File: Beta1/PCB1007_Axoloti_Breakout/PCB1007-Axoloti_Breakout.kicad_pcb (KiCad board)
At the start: 2 copper layers, 160 x 48 mm, 43 parts, among them J1 Axoloti_40Pin, U10 OLED_128x32_I2C, U1000 MCP3008T-I/SL, U2 MCP3008T-I/SL, U20 OLED_128x32_I2C, U30 OLED_128x32_I2C, U40 OLED_128x32_I2C, U5 I2C_1x4MUX_TCA9546A

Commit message: SCH+Route complete
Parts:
- removed C1, C1000, C2: 0.1u, Capacitors_SMD:C_0603
- removed JOY0, JOY1, JOY2, JOY3: XYJOY, Liberry:XY_JOY_254TA103B50B
- removed RC0, RC10, RC20, RC30, RC40, RD0, RD10, RD20, RD30, RD40, RR0: 10K, Resistors_SMD:R_0603
- removed the REF** at (44.0, -10.0)
- removed RV0, RV1, RV2, RV3, RV4, RV5, RV6, RV7, RV_VOL1: POT, Liberry:RV09AF-40-20K-B10K
- removed U10, U20, U30, U40: OLED_128x32_I2C, Liberry:OLED_128x32
- removed U1000, U2: MCP3008T-I/SL, Liberry:SOIC-16
- removed U5: I2C_1x4MUX_TCA9546A, Liberry:SOIC-16_1.27x5.4
- added JK0: USB-K, Liberry:USB-K_12401610E4_2A, F.Cu at (8.60, -25.4)
- added REF**: Fiducial_1mm_Dia_2.54mm_Outer_CopperTop, Fiducials:Fiducial_1mm_Dia_2.54mm_Outer_CopperTop, F.Cu at (12.7, -7.62)
- added REF**: Fiducial_1mm_Dia_2.54mm_Outer_CopperTop, Fiducials:Fiducial_1mm_Dia_2.54mm_Outer_CopperTop, F.Cu at (12.7, -35.6)
- added REF**: 1pin, Connect:1pin, F.Cu at (44.0, -10.0)
- added REF**: 1pin, Connect:1pin, F.Cu at (3.50, -10.0)
- added TEST0: CONN_01X01, Liberry:TH_0.1_1x2_Jumper, F.Cu at (22.9, -43.2)
- added TEST1: CONN_01X01, Liberry:TH_0.1_1x2_Jumper, F.Cu at (22.9, -45.7)
- added TEST2: CONN_01X01, Liberry:TH_0.1_1x2_Jumper, F.Cu at (22.9, -40.6)
- moved REF** 38.2 mm to (2.54, -35.6)
- moved REF** 30.0 mm to (3.50, -40.0)
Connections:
- J1 pad 11: /JOY_K0 -> /JOY0
- J1 pad 12: /JOY_K1 -> /JOY1
- J1 pad 18: Net-(J1-Pad18) -> /TX
- J1 pad 19: Net-(J1-Pad19) -> /RX
- J1 pad 8: /JOY_0_SW -> /JOY_SW
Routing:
- net +3V3: track 618.9 -> 275.5 mm
- net /P0: track 132.1 -> 0.00 mm, vias 1 -> 0
- net /JOY_0_1: track 125.4 -> 0.00 mm, vias 1 -> 0
- net /RX: track 0.00 -> 113.3 mm, vias 0 -> 1
- net /TX: track 0.00 -> 111.9 mm, vias 0 -> 1
- net /P1: track 108.5 -> 0.00 mm, vias 1 -> 0
- net GND: track 166.7 -> 59.3 mm, vias 3 -> 1
- net /JOY0: track 0.00 -> 106.4 mm, vias 0 -> 1
- net /JOY_0_0: track 101.9 -> 0.00 mm, vias 1 -> 0
- net /I2C_SDA3: track 99.3 -> 0.00 mm
- net /JOY1: track 0.00 -> 97.6 mm
- net /I2C_SCL3: track 95.8 -> 0.00 mm
- net /JOY_SW: track 0.00 -> 87.7 mm, vias 0 -> 1
- net /JOY_1_1: track 75.3 -> 0.00 mm, vias 1 -> 0
- net /P2: track 70.2 -> 0.00 mm, vias 3 -> 0
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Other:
- board text added: "PCB1007_USB-K Breakout 2017-07-08 https://github.com/Believotron/BelievotronWanderlustHardware"
- board text removed: "254TA103B50B"
- board text removed: "All R=10KΩ All C=0.1uF"
- board text removed: "MCP3008T-I/SL"
- board text removed: "PCB1005_KnobCore_2017-07-06 8CH Knobs + Vol + 4CH JoyXY + 4CH OLED https://github.com/Believotron/BelievotronWanderlustHardware"
- board text removed: "RV09AF-40-20K-B10K"
- board text removed: "TCA9546ADR"

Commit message: PCB1006 Ready for fab
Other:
- board text added: "PCB1007_USB-K Breakout 2017-07-11 https://github.com/Believotron/BelievotronWanderlustHardware"
- board text removed: "PCB1007_USB-K Breakout 2017-07-08 https://github.com/Believotron/BelievotronWanderlustHardware"
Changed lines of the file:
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@@
     (links 118)
     (no_connects 1)
-    (area -0.050001 -48.050001 160.050001 0.050001)
+    (area -14.398096 -50.8 185.860001 0.100001)
     (thickness 1.6)
     (drawings 17)
@@
       (drillshape 0)
       (scaleselection 1)
-      (outputdirectory PCB1005-KnobCore_Gerbers_2017-06-07/))
+      (outputdirectory PCB1007-Axoloti_USB-K_2017-07-11_Gerbers/))
   )
   (net 0 "")
@@
     (effects (font (size 1.15 1.15) (thickness 0.15)))
   )
-  (gr_text "PCB1007_USB-K Breakout 2017-07-08\nhttps://github.com/Believotron/BelievotronWanderlustHardware\n" (at 0.635 -2.54) (layer F.SilkS)
+  (gr_text "PCB1007_USB-K Breakout 2017-07-11\nhttps://github.com/Believotron/BelievotronWanderlustHardware\n" (at 0.635 -2.54) (layer F.SilkS)
     (effects (font (size 1 1) (thickness 0.15)) (justify left))
   )

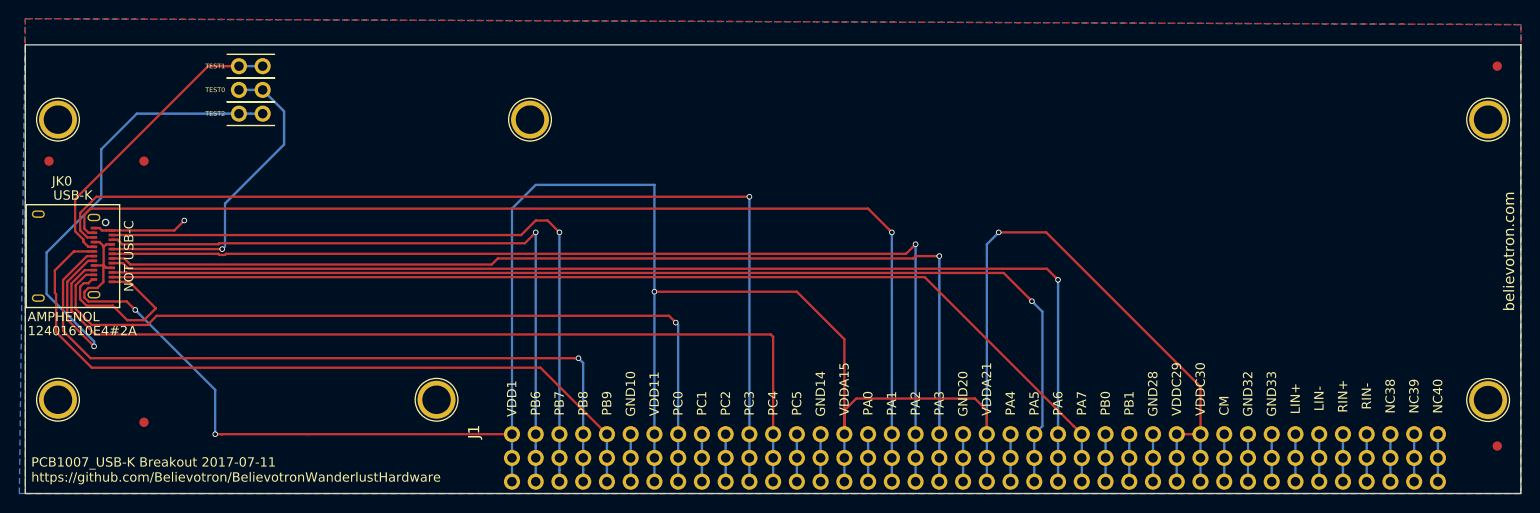
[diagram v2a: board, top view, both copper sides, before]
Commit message: Conversion to FFC WIP
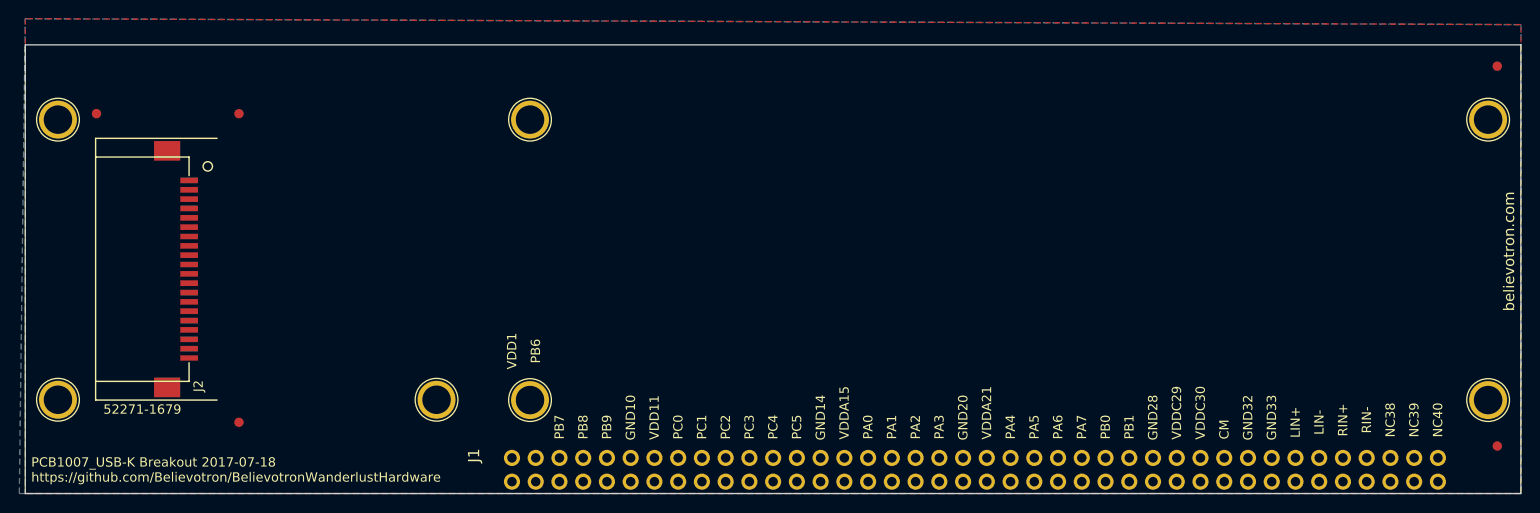
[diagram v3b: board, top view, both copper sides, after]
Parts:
- removed JK0: USB-K, Liberry:USB-K_12401610E4_2A
- removed TEST0, TEST1, TEST2: CONN_01X01, Liberry:TH_0.1_1x2_Jumper
- added J2: FPC_20POS, Liberry:FFC_1MM_20POS_MOLEX_52271-2079, F.Cu at (17.5, -24.0)
- added REF**: 1pin, Connect:1pin, F.Cu at (54.0, -10.0)
- J1: footprint Liberry:Axoloti-40x3_slim -> Liberry:Axoloti-40x2_slim
- moved REF** 11.4 mm to (22.9, -40.6)
- moved REF** 10.2 mm to (22.9, -7.62)
- moved REF** 7.18 mm to (7.62, -40.6)
- moved J1 2.54 mm to (52.1, -1.27)
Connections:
- net /JOY_2_SW renamed Net-(J1-Pad26)
- net /JOY_3_SW renamed Net-(J1-Pad27)
- net /JOY_K_SW renamed Net-(J1-Pad16)
- J1 pad 11: /JOY0 -> /JOY0_X
- J1 pad 12: /JOY1 -> /JOY0_Y
- J1 pad 13: Net-(J1-Pad13) -> /JOY0_SW
- J1 pad 22: Net-(J1-Pad22) -> /ANALOG_OUT
- J1 pad 8: /JOY_SW -> /PC0
- J1 pad 9: /JOY_1_SW -> /PC1
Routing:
- net +3V3: track 275.5 -> 0.00 mm, vias 4 -> 0
- net /SPI_MISO: track 123.6 -> 0.00 mm, vias 1 -> 0
- net /SPI_CLK: track 119.8 -> 0.00 mm, vias 1 -> 0
- net /VOLUME: track 117.1 -> 0.00 mm, vias 1 -> 0
- net /SPI_MOSI: track 115.8 -> 0.00 mm
- net /RX: track 113.3 -> 0.00 mm, vias 1 -> 0
- net /TX: track 111.9 -> 0.00 mm, vias 1 -> 0
- net /JOY0: track 106.4 -> 0.00 mm, vias 1 -> 0
- net /JOY1: track 97.6 -> 0.00 mm
- net /JOY_SW: track 87.7 -> 0.00 mm, vias 1 -> 0
- net /I2C_SDA: track 80.2 -> 0.00 mm
- net /I2C_SCL: track 79.6 -> 0.00 mm, vias 1 -> 0
- net /CS_0_7: track 75.7 -> 0.00 mm, vias 1 -> 0
- net /CS_8_15: track 72.7 -> 0.00 mm, vias 1 -> 0
- net GND: track 59.3 -> 0.00 mm, vias 1 -> 0
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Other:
- board text added: "PCB1007_USB-K Breakout 2017-07-18 https://github.com/Believotron/BelievotronWanderlustHardware"
- board text removed: "PCB1007_USB-K Breakout 2017-07-11 https://github.com/Believotron/BelievotronWanderlustHardware"

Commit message: Added 20 pos FFC
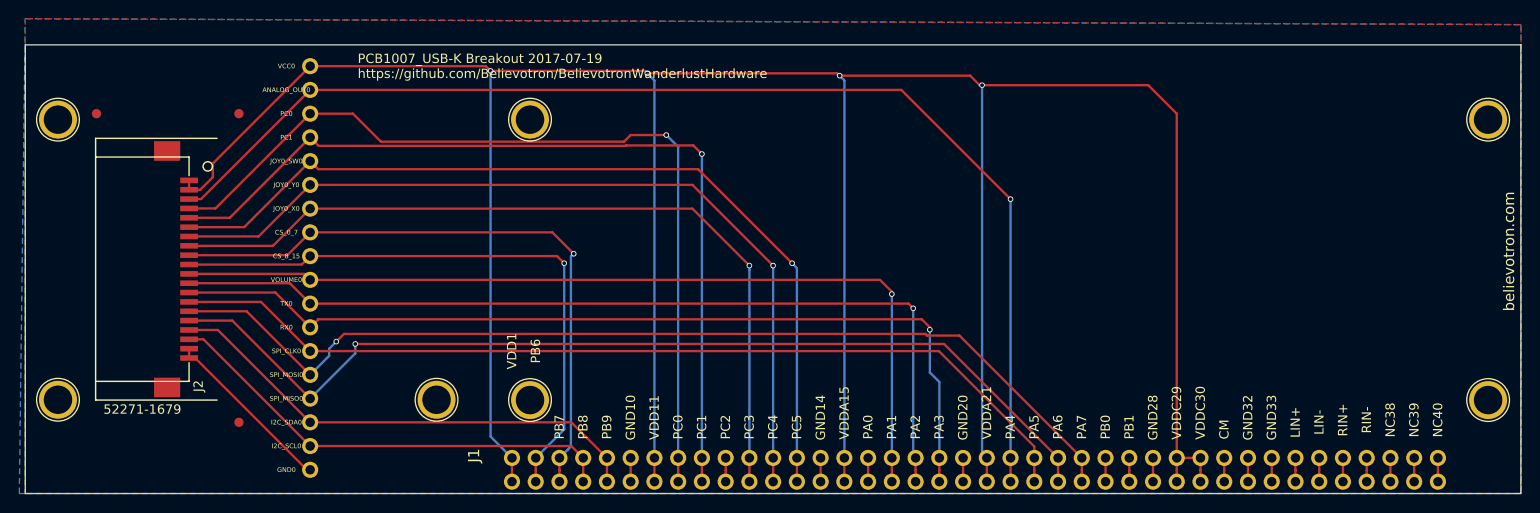
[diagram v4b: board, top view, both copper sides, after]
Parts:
- removed the REF** at (157.5, -5.08)
- removed the REF** at (157.5, -45.7)
- added ANALOG_OUT0: CONN_01X01, Liberry:single_0.1, F.Cu at (30.5, -43.2)
- added CS_0_7: CONN_01X01, Liberry:single_0.1, F.Cu at (30.5, -27.9)
- added CS_8_15: CONN_01X01, Liberry:single_0.1, F.Cu at (30.5, -25.4)
- added GND0: CONN_01X01, Liberry:single_0.1, F.Cu at (30.5, -2.54)
- added I2C_SCL0: CONN_01X01, Liberry:single_0.1, F.Cu at (30.5, -5.08)
- added I2C_SDA0: CONN_01X01, Liberry:single_0.1, F.Cu at (30.5, -7.62)
- added JOY0_SW0: CONN_01X01, Liberry:single_0.1, F.Cu at (30.5, -35.6)
- added JOY0_X0: CONN_01X01, Liberry:single_0.1, F.Cu at (30.5, -30.5)
- added JOY0_Y0: CONN_01X01, Liberry:single_0.1, F.Cu at (30.5, -33.0)
- added PC0: CONN_01X01, Liberry:single_0.1, F.Cu at (30.5, -40.6)
- added PC1: CONN_01X01, Liberry:single_0.1, F.Cu at (30.5, -38.1)
- added RX0: CONN_01X01, Liberry:single_0.1, F.Cu at (30.5, -17.8)
- added SPI_CLK0: CONN_01X01, Liberry:single_0.1, F.Cu at (30.5, -15.2)
- added SPI_MISO0: CONN_01X01, Liberry:single_0.1, F.Cu at (30.5, -10.2)
- added SPI_MOSI0: CONN_01X01, Liberry:single_0.1, F.Cu at (30.5, -12.7)
- added TX0: CONN_01X01, Liberry:single_0.1, F.Cu at (30.5, -20.3)
- added VCC0: CONN_01X01, Liberry:single_0.1, F.Cu at (30.5, -45.7)
- added VOLUME0: CONN_01X01, Liberry:single_0.1, F.Cu at (30.5, -22.9)
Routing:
- net +3V3: track 0.00 -> 334.7 mm, vias 0 -> 4
- net /ANALOG_OUT: track 0.00 -> 127.8 mm, vias 0 -> 1
- net /SPI_MOSI: track 0.00 -> 108.6 mm, vias 0 -> 1
- net /SPI_MISO: track 0.00 -> 107.0 mm, vias 0 -> 1
- net /SPI_CLK: track 0.00 -> 100.6 mm
- net /RX: track 0.00 -> 98.4 mm, vias 0 -> 1
- net /TX: track 0.00 -> 97.2 mm, vias 0 -> 1
- net /VOLUME: track 0.00 -> 96.3 mm, vias 0 -> 1
- net /JOY0_SW: track 0.00 -> 95.5 mm, vias 0 -> 1
- net /PC0: track 0.00 -> 94.4 mm, vias 0 -> 1
- net /PC1: track 0.00 -> 94.3 mm, vias 0 -> 1
- net /JOY0_Y: track 0.00 -> 91.5 mm, vias 0 -> 1
- net /JOY0_X: track 0.00 -> 87.2 mm, vias 0 -> 1
- net /CS_0_7: track 0.00 -> 68.1 mm, vias 0 -> 1
- net /CS_8_15: track 0.00 -> 65.5 mm, vias 0 -> 1
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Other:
- board text added: "PCB1007_USB-K Breakout 2017-07-19 https://github.com/Believotron/BelievotronWanderlustHardware"
- board text removed: "PCB1007_USB-K Breakout 2017-07-18 https://github.com/Believotron/BelievotronWanderlustHardware"

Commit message: Ready for fab
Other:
- board text added: "PCB1007_FPC Breakout 2017-07-19 https://github.com/Believotron/BelievotronWanderlustHardware"
- board text removed: "PCB1007_USB-K Breakout 2017-07-19 https://github.com/Believotron/BelievotronWanderlustHardware"
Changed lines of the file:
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@@
     (links 88)
     (no_connects 0)
-    (area -0.050001 -48.050001 160.050001 0.050001)
+    (area -9.318096 -50.8 185.860001 1.075)
     (thickness 1.6)
     (drawings 17)
@@
       (drillshape 0)
       (scaleselection 1)
-      (outputdirectory PCB1007-Axoloti_USB-K_2017-07-11_Gerbers/))
+      (outputdirectory Output/PCB1007-2017-07-19_Gerbers/))
   )
   (net 0 "")
@@
     (effects (font (size 1.15 1.15) (thickness 0.15)))
   )
-  (gr_text "PCB1007_USB-K Breakout 2017-07-19\nhttps://github.com/Believotron/BelievotronWanderlustHardware\n" (at 35.56 -45.72) (layer F.SilkS)
+  (gr_text "PCB1007_FPC Breakout 2017-07-19\nhttps://github.com/Believotron/BelievotronWanderlustHardware\n" (at 35.56 -45.72) (layer F.SilkS)
     (effects (font (size 1 1) (thickness 0.15)) (justify left))
   )

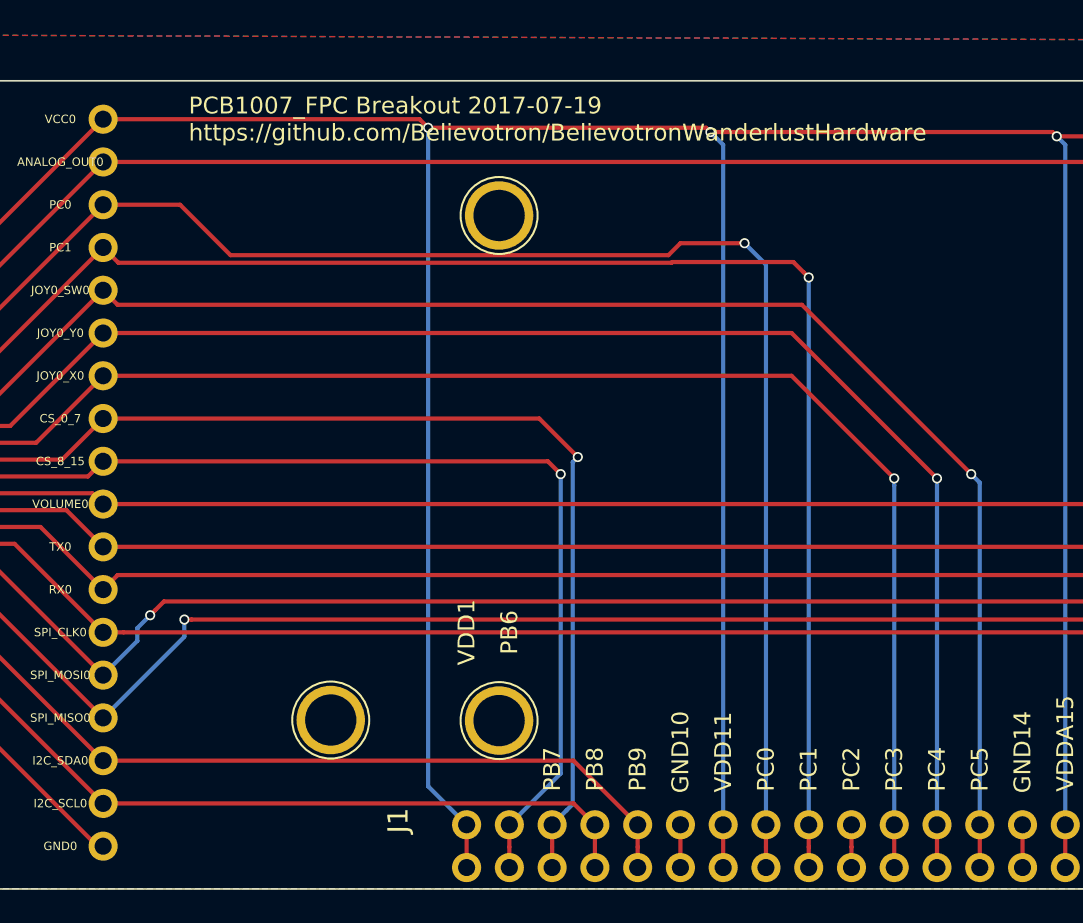
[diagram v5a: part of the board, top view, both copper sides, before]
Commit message: Changed con pinout. Ready for Fab.
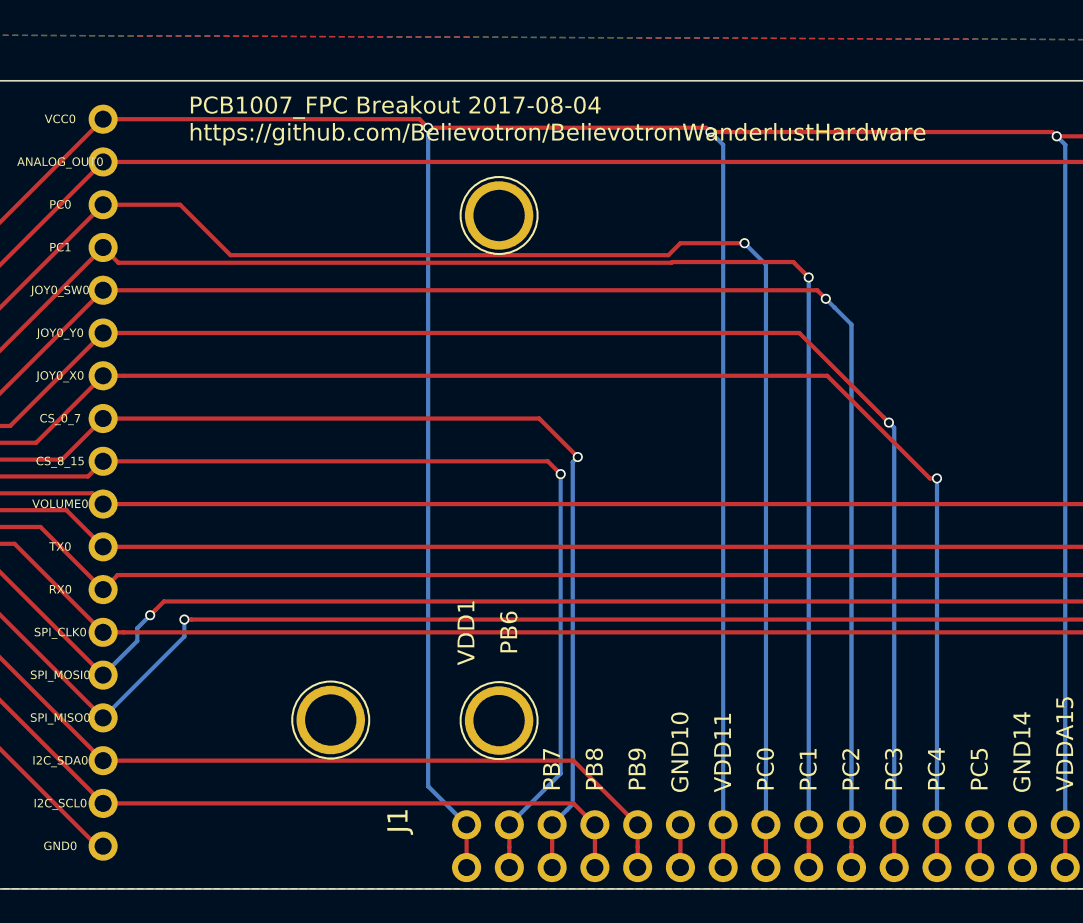
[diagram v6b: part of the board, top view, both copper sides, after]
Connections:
- J1 pad 10: /!OLED_RESET -> /JOY0_SW
- J1 pad 11: /JOY0_X -> /JOY0_Y
- J1 pad 12: /JOY0_Y -> /JOY0_X
- J1 pad 13: /JOY0_SW -> Net-(J1-Pad13)
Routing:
- net /JOY0_X: track 87.2 -> 89.8 mm
- net Net-(J1-Pad13): track 0.00 -> 2.54 mm
- net /!OLED_RESET: track 2.54 -> 0.00 mm
- net /JOY0_SW: track 95.5 -> 93.4 mm
- net /JOY0_Y: track 91.5 -> 90.7 mm
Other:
- board text added: "PCB1007_FPC Breakout 2017-08-04 https://github.com/Believotron/BelievotronWanderlustHardware"
- board text removed: "PCB1007_FPC Breakout 2017-07-19 https://github.com/Believotron/BelievotronWanderlustHardware"
